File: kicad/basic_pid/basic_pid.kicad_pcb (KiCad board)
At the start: 2 copper layers, 9 parts, among them U1 LM4040LP-5, U10 OPA189, U11 BUF634A, U2 LM4040LP-5, U5 OPA189, U6 OPA189, U7 OPA189, U8 OPA189, U9 OPA189

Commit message: Schematic almost finalized:
Ended up using switches to select pre-set capacitors rather than ZIFs

TO DO:
1) design the power supply and filtering section.
2) Layout work (consider adding capacitors for stabilization...)
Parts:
- removed the U11 at (109.6, 87.7)
- added C1: 100p, Capacitor_SMD:C_0805_2012Metric, F.Cu at (130.8, 57.4)
- added C10: 100p, Capacitor_SMD:C_0805_2012Metric, F.Cu at (159.9, 130.0)
- added C11: 1n, Capacitor_SMD:C_0805_2012Metric, F.Cu at (159.9, 132.3)
- added C12: 10n, Capacitor_SMD:C_0805_2012Metric, F.Cu at (160.0, 134.6)
- added C13: 100nF, Capacitor_SMD:C_0805_2012Metric, F.Cu at (95.5, 122.0)
- added C14: 100nF, Capacitor_SMD:C_0805_2012Metric, F.Cu at (95.5, 125.0)
- added C15: 100nF, Capacitor_SMD:C_0805_2012Metric, F.Cu at (95.5, 128.0)
- added C16: 100nF, Capacitor_SMD:C_0805_2012Metric, F.Cu at (95.5, 131.0)
- added C17: 100nF, Capacitor_SMD:C_0805_2012Metric, F.Cu at (95.5, 134.1)
- added C18: 100nF, Capacitor_SMD:C_0805_2012Metric, F.Cu at (95.5, 137.1)
- added C19: 100nF, Capacitor_SMD:C_0805_2012Metric, F.Cu at (99.9, 122.0)
- added C2: 1n, Capacitor_SMD:C_0805_2012Metric, F.Cu at (130.8, 69.5)
- added C20: 100nF, Capacitor_SMD:C_0805_2012Metric, F.Cu at (99.9, 125.0)
- added C21: 100nF, Capacitor_SMD:C_0805_2012Metric, F.Cu at (99.9, 128.0)
- added C22: 100nF, Capacitor_SMD:C_0805_2012Metric, F.Cu at (99.9, 131.0)
- added C23: 100nF, Capacitor_SMD:C_0805_2012Metric, F.Cu at (99.9, 134.1)
- added C24: 100nF, Capacitor_SMD:C_0805_2012Metric, F.Cu at (99.9, 137.1)
- added C25: 100nF, Capacitor_SMD:C_0805_2012Metric, F.Cu at (104.4, 122.0)
- added C26: 100nF, Capacitor_SMD:C_0805_2012Metric, F.Cu at (104.4, 125.0)
- added C27: 100nF, Capacitor_SMD:C_0805_2012Metric, F.Cu at (104.4, 128.0)
- added C28: 100nF, Capacitor_SMD:C_0805_2012Metric, F.Cu at (104.4, 131.0)
- added C29: 100nF, Capacitor_SMD:C_0805_2012Metric, F.Cu at (104.4, 134.1)
- added C3: 10n, Capacitor_SMD:C_0805_2012Metric, F.Cu at (130.8, 75.5)
- added C30: 100nF, Capacitor_SMD:C_0805_2012Metric, F.Cu at (104.4, 137.1)
- added C31: 100nF, Capacitor_SMD:C_0805_2012Metric, F.Cu at (108.8, 122.0)
- added C32: 100nF, Capacitor_SMD:C_0805_2012Metric, F.Cu at (108.8, 125.0)
- added C33: 100nF, Capacitor_SMD:C_0805_2012Metric, F.Cu at (108.8, 128.0)
- added C34: 100nF, Capacitor_SMD:C_0805_2012Metric, F.Cu at (108.8, 131.0)
- added C35: 100n, Capacitor_SMD:C_0805_2012Metric, F.Cu at (65.7, 160.8)
- added C36: 100nF, Capacitor_SMD:C_0805_2012Metric, F.Cu at (-52.9, -24.3)
- added C37: 100nF, Capacitor_SMD:C_0805_2012Metric, F.Cu at (-52.9, -21.3)
- added C38: 100nF, Capacitor_SMD:C_0805_2012Metric, F.Cu at (63.9, 43.5)
- added C4: 100n, Capacitor_SMD:C_0805_2012Metric, F.Cu at (130.8, 81.6)
- added C5: 100p, Capacitor_SMD:C_0805_2012Metric, F.Cu at (164.7, -151.9)
- added C6: 1n, Capacitor_SMD:C_0805_2012Metric, F.Cu at (164.6, -149.7)
- added C7: 10n, Capacitor_SMD:C_0805_2012Metric, F.Cu at (164.6, -147.4)
- added C8: 100n, Capacitor_SMD:C_0805_2012Metric, F.Cu at (163.3, -145.1)
- added C9: DNP, Capacitor_SMD:C_0805_2012Metric, F.Cu at (159.9, 127.8)
- added J1: Input A, lib:BNC_Amphenol_B6252HB-NPP3G-50_Horizontal, B.Cu at (245.1, 52.6)
- added J2: Input B / Setpoint, lib:BNC_Amphenol_B6252HB-NPP3G-50_Horizontal, F.Cu at (166.2, 88.7)
- added J3: Output, lib:BNC_Amphenol_B6252HB-NPP3G-50_Horizontal, F.Cu at (183.0, 88.7)
- added J4: Output, lib:BNC_Amphenol_B6252HB-NPP3G-50_Horizontal, F.Cu at (199.7, 88.7)
- added R1: R_US, Resistor_SMD:R_0805_2012Metric, F.Cu at (65.6, 143.1)
- added R10: 10k, Resistor_SMD:R_0805_2012Metric, F.Cu at (163.7, -196.1)
- added R11: 10k, Resistor_SMD:R_0805_2012Metric, F.Cu at (384.9, -129.3)
- added R12: 220, Resistor_SMD:R_0805_2012Metric, F.Cu at (70.1, 157.8)
- added R13: 50, Resistor_SMD:R_0805_2012Metric, F.Cu at (74.5, 143.1)
- added R14: 10M, Resistor_SMD:R_0805_2012Metric, F.Cu at (178.0, -147.6)
- added R15: 10k, Resistor_SMD:R_0805_2012Metric, F.Cu at (74.5, 149.0)
- added R16: 10k, Resistor_SMD:R_0805_2012Metric, F.Cu at (74.5, 151.9)
- added R17: 10k, Resistor_SMD:R_0805_2012Metric, F.Cu at (74.5, 154.9)
- added R18: 10k, Resistor_SMD:R_0805_2012Metric, F.Cu at (74.5, 157.8)
- added R19: 50, Resistor_SMD:R_0805_2012Metric, F.Cu at (78.9, 143.1)
- added R2: R_US, Resistor_SMD:R_0805_2012Metric, F.Cu at (65.6, 146.0)
- added R20: 10k, Resistor_SMD:R_0805_2012Metric, F.Cu at (78.9, 146.0)
- added R21: 10k, Resistor_SMD:R_0805_2012Metric, F.Cu at (78.9, 149.0)
- added R22: 1M, Resistor_SMD:R_0805_2012Metric, F.Cu at (178.0, -149.9)
- added R23: 1k, Resistor_SMD:R_0805_2012Metric, F.Cu at (137.3, 129.4)
- added R24: 1k, Resistor_SMD:R_0805_2012Metric, F.Cu at (137.3, 132.4)
- added R25: 1k, Resistor_SMD:R_0805_2012Metric, F.Cu at (137.3, 135.3)
- added R26: 1k, Resistor_SMD:R_0805_2012Metric, F.Cu at (137.3, 138.3)
- added R27: 1k, Resistor_SMD:R_0805_2012Metric, F.Cu at (137.3, 141.2)
- added R28: 10, Resistor_SMD:R_0805_2012Metric, F.Cu at (-65.8, -24.3)
- added R29: 10, Resistor_SMD:R_0805_2012Metric, F.Cu at (-65.8, -21.4)
- added R3: 10k, Resistor_SMD:R_0805_2012Metric, F.Cu at (65.6, 149.0)
- added R30: 10k, Resistor_SMD:R_0805_2012Metric, F.Cu at (-65.8, -18.4)
- added R31: 10k, Resistor_SMD:R_0805_2012Metric, F.Cu at (-65.8, -15.5)
- added R32: 10k, Resistor_SMD:R_0805_2012Metric, F.Cu at (-65.8, -12.5)
- added R33: 10k, Resistor_SMD:R_0805_2012Metric, F.Cu at (72.0, 28.4)
- added R34: 1k, Resistor_SMD:R_0805_2012Metric, F.Cu at (51.0, 52.2)
- added R4: 10k, Resistor_SMD:R_0805_2012Metric, F.Cu at (65.6, 151.9)
- added R5: 10k, Resistor_SMD:R_0805_2012Metric, F.Cu at (65.6, 154.9)
- added R6: 10k, Resistor_SMD:R_0805_2012Metric, F.Cu at (65.6, 157.8)
- added R7: 10k, Resistor_SMD:R_0805_2012Metric, F.Cu at (70.1, 143.1)
- added R8: 10k, Resistor_SMD:R_0805_2012Metric, F.Cu at (70.1, 146.0)
- added R9: 10k, Resistor_SMD:R_0805_2012Metric, F.Cu at (70.1, 149.0)
- added RV1: 100k, lib:Slide_pot_45mm, B.Cu at (45.7, 149.4)
- added RV2: 100k, lib:Slide_pot_45mm, B.Cu at (170.9, -168.4)
- added RV3: 100k, lib:Slide_pot_45mm, B.Cu at (391.9, -101.9)
- added RV4: 100k, lib:Slide_pot_45mm, F.Cu at (238.6, 124.6)
- added RV5: 100k, lib:Slide_pot_45mm, F.Cu at (250.7, 124.6)
- added RV6: 100k, lib:Slide_pot_45mm, F.Cu at (58.4, 151.1)
- added RV7: 10K, Potentiometer_THT:Potentiometer_Bourns_3296W_Vertical, F.Cu at (-60.5, -4.93)
- added RV9: 10K, Potentiometer_THT:Potentiometer_Bourns_3296W_Vertical, F.Cu at (61.0, 23.9)
- added SW1: SW_DPDT_x2, lib:MHS222, B.Cu at (245.9, 60.1)
- added SW10: SW_DPDT_x2, lib:MHS222, F.Cu at (58.3, 31.5)
- added SW2: SW_DPDT_x2, lib:MHS222, F.Cu at (193.9, 133.0)
- added SW4: SW_SP4T, lib:SLB1470, F.Cu at (144.2, 102.5)
- added SW6: SW_SP4T, lib:SLB1470, F.Cu at (150.3, 102.5)
- added SW7: SW_SP4T, lib:SLB1470, B.Cu at (160.0, -148.5)
- added SW8: SW_SP4T, lib:SLB1470, B.Cu at (181.3, -148.6)
- added SW9: SW_SP4T, lib:SLB1470, F.Cu at (155.4, 131.3)
- added U13: BUF634A, lib:TI_SO-PowerPAD-8_ThermalVias, F.Cu at (162.3, 139.1)
- added U14: OPA189, Package_SO:SOIC-8_3.9x4.9mm_P1.27mm, F.Cu at (-59.4, -22.6)
- added U15: OPA189, Package_SO:SOIC-8_3.9x4.9mm_P1.27mm, F.Cu at (-59.4, -16.1)
- added U3: LT1167, Package_DIP:DIP-8_W7.62mm_LongPads, B.Cu at (241.8, 66.8)
- added U4: LT1167, Package_DIP:DIP-8_W7.62mm_LongPads, F.Cu at (181.6, 94.0)
- added U7: OPA189, Package_SO:SOIC-8_3.9x4.9mm_P1.27mm, F.Cu at (172.3, 106.9)
- added U8: BUF634A, lib:TI_SO-PowerPAD-8_ThermalVias, F.Cu at (163.7, 101.7)
- moved U10 362.8 mm to (390.0, -123.3), turned to -90 degrees
- moved U9 245.7 mm to (170.3, -146.6), turned to 90 degrees
- moved U5 83.3 mm to (45.5, 138.6)
- moved U12 72.0 mm to (162.4, 145.4)
- renumbered U8 to U10, U9 to U11, U10 to U12, U7 to U9
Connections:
- U12 pad 4: VS -> Vlim-
- U12 pad 7: VD -> Vlim+
- U5 pad 6: Net-(U5--) -> Internal_setpoint
- U6 pad 6: Net-(J3-In) -> Error_signal
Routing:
- net Net-(SW7-Common): track 0.00 -> 58.4 mm
- net Net-(R17-Pad1): track 0.00 -> 47.0 mm, vias 0 -> 2
- net Net-(C5-Pad1): track 0.00 -> 36.6 mm
- net Net-(J1-In): track 0.00 -> 23.8 mm
- net Net-(J1-Ext): track 0.00 -> 20.3 mm
- net Net-(SW1A-B): track 0.00 -> 10.2 mm
- net Net-(U10--): track 0.00 -> 8.44 mm
- net Net-(SW1B-B): track 0.00 -> 6.28 mm
- net Net-(C5-Pad2): track 0.00 -> 3.71 mm
- net Net-(C6-Pad2): track 0.00 -> 3.69 mm
- net Net-(C7-Pad2): track 0.00 -> 3.64 mm
- net Net-(R14-Pad1): track 0.00 -> 2.44 mm
- net Net-(R22-Pad1): track 0.00 -> 2.43 mm
- net Net-(C8-Pad2): track 0.00 -> 2.36 mm
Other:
- copper layers 2 -> 4

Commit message: Schematic finalized and layout work begun
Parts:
- removed RV9: 10K, Potentiometer_THT:Potentiometer_Bourns_3296W_Vertical
- added C39: 100nF, Capacitor_SMD:C_0805_2012Metric, F.Cu at (156.2, 184.9)
- added C40: 100nF, Capacitor_SMD:C_0805_2012Metric, F.Cu at (148.7, 214.6)
- added C41: 100nF, Capacitor_SMD:C_0805_2012Metric, F.Cu at (49.4, 67.7)
- added C42: 10uF, Capacitor_SMD:C_1210_3225Metric, F.Cu at (54.4, 68.3)
- added C43: 100nF, Capacitor_SMD:C_0805_2012Metric, F.Cu at (49.4, 70.7)
- added C44: 22uF, Capacitor_SMD:CP_Elec_4x5.8, F.Cu at (51.0, 63.3)
- added D1: GBU4A, Diode_THT:Diode_Bridge_Vishay_GBU, F.Cu at (118.6, 199.9)
- added H1: MountingHole, MountingHole:MountingHole_3.2mm_M3_ISO14580, F.Cu at (101.6, 29.6)
- added H2: MountingHole, MountingHole:MountingHole_3.2mm_M3_ISO14580, F.Cu at (101.6, 36.7)
- added H3: MountingHole, MountingHole:MountingHole_3.2mm_M3_ISO14580, F.Cu at (101.6, 43.8)
- added H4: MountingHole, MountingHole:MountingHole_3.2mm_M3_ISO14580, F.Cu at (101.6, 50.8)
- added J5: Screw_Terminal_01x04, TerminalBlock:TerminalBlock_Altech_AK300-4_P5.00mm, F.Cu at (35.1, 55.5)
- added J6: Screw_Terminal_01x03, TerminalBlock:TerminalBlock_Altech_AK300-3_P5.00mm, F.Cu at (73.6, 57.9)
- added SW3: SW_DPDT_x2, lib:MHS222, F.Cu at (40.1, 81.6)
- added SW5: SW_DPDT_x2, lib:MHS222, F.Cu at (40.1, 90.6)
- added U16: LM317_TO-252, Package_TO_SOT_SMD:TO-252-2, F.Cu at (41.9, 64.4)
- C1: value 100p -> 100n
- C10: value 100p -> DNP
- C11: value 1n -> 100p
- C12: value 10n -> 1n
- C13: value 100nF -> 10n
- C18, C19: value 100nF -> 22mF; footprint Capacitor_SMD:C_0805_2012Metric -> Capacitor_THT:CP_Radial_D30.0mm_P10.00mm_SnapIn
- C2: value 1n -> DNP
- C24, C25: value 100nF -> 10uF; footprint Capacitor_SMD:C_0805_2012Metric -> Capacitor_SMD:C_1210_3225Metric
- C3: value 10n -> 100p
- C32, C33: value 100nF -> 220uF; footprint Capacitor_SMD:C_0805_2012Metric -> Capacitor_SMD:CP_Elec_8x6.9
- C35, C8: value 100n -> 100nF
- C4: value 100n -> 1n
- C5: value 100p -> 10n
- C6: value 1n -> 1nF
- C7: value 10n -> 10nF
- C9: value DNP -> 1uF
- J1, J3, J4: footprint lib:BNC_Amphenol_B6252HB-NPP3G-50_Horizontal -> lib:BNC_Amphenol_031-5539_Vertical
- J2: footprint lib:BNC_Amphenol_B6252HB-NPP3G-50_Horizontal -> lib:BNC_Amphenol_031-5539_Vertical; moved to B.Cu
- R12: value 220 -> 10k
- R13, R19: value 50 -> 10k
- R14: value 10M -> 220
- R15: value 10k -> 50
- R16: value 10k -> 1M
- R17: value 10k -> 10M
- R22: value 1M -> 10k
- R23: value 1k -> 50
- R28: value 10 -> 1k
- R29: value 10 -> DNP
- R30, R31: value 10k -> 1k
- R32: value 10k -> 330
- R33: value 10k -> DNP
- R34: value 1k -> DNP
- RV6: value 100k -> 10K; footprint lib:Slide_pot_45mm -> Potentiometer_THT:Potentiometer_Bourns_3296W_Vertical
- RV7: value 10K -> 2k
- SW2, U4: moved to B.Cu
- U14: value OPA189 -> LM2940CS-12/NOPB; footprint Package_SO:SOIC-8_3.9x4.9mm_P1.27mm -> Package_TO_SOT_SMD:TO-263-3_TabPin2
- U15: value OPA189 -> LM2990SX-12; footprint Package_SO:SOIC-8_3.9x4.9mm_P1.27mm -> Package_TO_SOT_SMD:TO-263-3_TabPin2
- moved C37 282.5 mm to (93.7, 220.1)
- moved U15 277.7 mm to (125.2, 191.3)
- moved U14 273.3 mm to (125.2, 179.0)
- moved C36 258.5 mm to (93.7, 188.6)
- moved RV3 243.0 mm to (195.0, 40.4)
- moved R11 243.0 mm to (188.0, 13.0)
- moved U10 243.0 mm to (193.1, 19.0)
- moved C5 207.5 mm to (152.6, 55.2)
- moved C6 207.5 mm to (152.6, 57.4)
- moved C7 207.5 mm to (152.5, 59.8)
- moved C8 207.5 mm to (151.3, 62.1)
- moved R10 207.5 mm to (151.6, 11.0)
- moved R14 207.5 mm to (165.9, 59.6)
- moved R22 207.5 mm to (165.9, 57.3)
- moved RV2 207.5 mm to (158.8, 38.7)
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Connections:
- C1 pad 1: Net-(SW5-B) -> GND
- C13 pad 1: VD -> Net-(U13-OUT)
- C13 pad 2: GND -> Net-(C13-Pad2)
- C14 pad 1: GND -> +12V
- C14 pad 2: VS -> GND
- C15 pad 1: VD -> GND
- C15 pad 2: GND -> -12V
- C16 pad 1: GND -> +12V
- C16 pad 2: VS -> GND
- C17 pad 1: VD -> GND
- C17 pad 2: GND -> -12V
- C18 pad 1: GND -> V+_unreg
- C18 pad 2: VS -> GND
- C19 pad 1: VD -> GND
- C19 pad 2: GND -> Net-(D1--)
- C2 pad 1: Net-(SW5-B) -> Net-(SW3A-B)
- C20 pad 1: GND -> +12V
- C20 pad 2: VS -> GND
- C21 pad 1: VD -> GND
- C21 pad 2: GND -> -12V
- C22 pad 1: GND -> +12V
- C22 pad 2: VS -> GND
- C23 pad 1: VD -> GND
- C23 pad 2: GND -> -12V
- C24 pad 1: GND -> V+_unreg
- C24 pad 2: VS -> GND
- C25 pad 1: VD -> GND
- C25 pad 2: GND -> Net-(D1--)
- C26 pad 1: GND -> +12V
- C26 pad 2: VS -> GND
- C27 pad 1: VD -> GND
- C27 pad 2: GND -> -12V
- C28 pad 1: GND -> +12V
- C28 pad 2: VS -> GND
- C29 pad 1: VD -> GND
- C29 pad 2: GND -> -12V
- C3 pad 1: Net-(SW5-B) -> Net-(SW3A-B)
- C30 pad 1: GND -> +12V
- C30 pad 2: VS -> GND
- C31 pad 1: VD -> GND
- C31 pad 2: GND -> -12V
- C32 pad 1: GND -> +12V
- C32 pad 2: VS -> GND
- C33 pad 1: VD -> GND
- C33 pad 2: GND -> -12V
- C34 pad 1: GND -> +12V
- C34 pad 2: VS -> GND
- C35 pad 2: Net-(C35-Pad2) -> -12V
- C36 pad 1: Net-(C36-Pad1) -> +12V
- C36 pad 2: unconnected-(C36-Pad2) -> GND
- C37 pad 1: Net-(C37-Pad1) -> GND
- C37 pad 2: unconnected-(C37-Pad2) -> -12V
- C38 pad 1: Vlim- -> +12V
- C4 pad 1: Net-(SW5-B) -> Net-(SW3A-B)
- C5 pad 1: Net-(C5-Pad1) -> Net-(SW3A-B)
- C6 pad 1: Net-(C5-Pad1) -> Net-(C6-Pad1)
- C7 pad 1: Net-(C5-Pad1) -> Net-(C6-Pad1)
- C8 pad 1: Net-(C5-Pad1) -> Net-(C6-Pad1)
- C9 pad 1: Net-(U13-OUT) -> Net-(C6-Pad1)
- R1 pad 2: VD -> +12V
- R10 pad 1: Error_signal -> Net-(R10-Pad1)
- R10 pad 2: Net-(R10-Pad2) -> Error_signal
- R11 pad 1: Error_signal -> Net-(R11-Pad1)
- R11 pad 2: Net-(U10--) -> Net-(R10-Pad1)
- R12 pad 1: Net-(SW6-Common) -> Error_signal
- R12 pad 2: Net-(U11--) -> Net-(R12-Pad2)
- R13 pad 1: Net-(U7--) -> Error_signal
- R13 pad 2: Net-(J3-In) -> Net-(U10--)
- R14 pad 1: Net-(R14-Pad1) -> Net-(SW6-Common)
- R14 pad 2: Net-(C5-Pad1) -> Net-(U11--)
- R15 pad 1: Net-(R15-Pad1) -> Net-(U7--)
- R15 pad 2: Net-(SW9-Common) -> Net-(J3-In)
- R16 pad 1: Net-(C5-Pad1) -> Net-(R16-Pad1)
- R16 pad 2: Net-(SW9-Common) -> Net-(C6-Pad1)
- R17 pad 2: Net-(SW9-Common) -> Net-(C6-Pad1)
- R18 pad 1: Net-(SW9-Common) -> Net-(R18-Pad1)
- R18 pad 2: Net-(U13-OUT) -> Net-(SW9-Common)
- R19 pad 1: Net-(U13-OUT) -> Net-(C6-Pad1)
- R19 pad 2: Net-(J4-In) -> Net-(SW9-Common)
- R2 pad 1: VS -> -12V
- R20 pad 1: Net-(U5--) -> Net-(R20-Pad1)
- R20 pad 2: Internal_setpoint -> Net-(SW9-Common)
- R21 pad 1: GND -> Net-(SW9-Common)
- R21 pad 2: Net-(U5--) -> Positive_offset
- R22 pad 1: Net-(R22-Pad1) -> Net-(SW9-Common)
- R22 pad 2: Net-(C5-Pad1) -> Net-(U13-OUT)
- R23 pad 1: Net-(R23-Pad1) -> Net-(U13-OUT)
- R23 pad 2: VD -> Net-(J4-In)
- R24 pad 2: VD -> +12V
- R25 pad 2: VD -> +12V
- R26 pad 1: VS -> Net-(R26-Pad1)
- R26 pad 2: Net-(R26-Pad2) -> +12V
- R27 pad 1: VS -> -12V
- R28 pad 1: Net-(C36-Pad1) -> -12V
- R29 pad 1: Net-(C37-Pad1) -> -12V
- R29 pad 2: Net-(U15--) -> Net-(SW10A-C)
- R3 pad 1: Net-(C35-Pad2) -> Net-(C1-Pad2)
- R30 pad 1: VD -> Net-(R30-Pad1)
- R30 pad 2: Net-(R30-Pad2) -> Net-(U16-ADJ)
- R31 pad 1: Net-(R28-Pad2) -> -12V
- R31 pad 2: Net-(U14--) -> Vlim-
- R32 pad 1: Net-(U14--) -> Net-(U16-ADJ)
- R32 pad 2: GND -> Vlim+
- R33 pad 1: Net-(SW9-Common) -> Net-(R33-Pad1)
- R33 pad 2: Positive_offset -> Net-(R33-Pad2)
- R34 pad 1: VS -> Net-(R34-Pad1)
- R34 pad 2: Vlim- -> Net-(R34-Pad2)
- R4 pad 1: Input_B -> GND
- R4 pad 2: Net-(U6-+) -> Net-(U5--)
- R5 pad 1: Internal_setpoint -> Net-(U5--)
- R5 pad 2: Net-(U6-+) -> Internal_setpoint
- R6 pad 1: Input_A -> Input_B
- R7 pad 1: GND -> Internal_setpoint
- R7 pad 2: Net-(U6--) -> Net-(U6-+)
- R8 pad 1: Net-(R8-Pad1) -> Input_A
- R8 pad 2: Error_signal -> Net-(U6-+)
- R9 pad 1: Net-(R9-Pad1) -> GND
- R9 pad 2: Net-(R8-Pad1) -> Net-(U6--)
- RV1 pad 1: Net-(R9-Pad1) -> Net-(U1-K)
- RV1 pad 2: Net-(U6--) -> Net-(C1-Pad2)
- RV1 pad 3: Net-(U6--) -> Net-(U2-A)
- RV1 pad A: Net-(R23-Pad1) -> GND
- RV1 pad C: GND -> Net-(R28-Pad2)
- RV2 pad 1: Net-(R10-Pad2) -> Net-(R11-Pad1)
- RV2 pad 2: Net-(R10-Pad2) -> Net-(U6--)
- RV2 pad 3: Net-(SW7-Common) -> Net-(U6--)
- RV3 pad 1: Net-(U10--) -> Net-(R12-Pad2)
- RV3 pad 2: Net-(U10--) -> Net-(R12-Pad2)
- RV3 pad 3: Net-(R17-Pad1) -> Net-(SW7-Common)
- RV4 pad 1: Net-(R15-Pad1) -> Net-(U10--)
- RV4 pad 2: Net-(U11--) -> Net-(U10--)
- RV4 pad 3: Net-(U11--) -> Net-(R20-Pad1)
- RV4 pad A: GND -> Net-(R26-Pad1)
- RV4 pad C: Net-(R26-Pad2) -> GND
- RV5 pad 1: (no net) -> Net-(R18-Pad1)
- RV5 pad 2: (no net) -> Net-(U11--)
- RV5 pad 3: (no net) -> Net-(U11--)
- RV6 pad 1: Net-(U1-K) -> GND
- RV6 pad 2: Net-(C35-Pad2) -> Net-(SW10A-C)
- RV6 pad 3: Net-(U2-A) -> -12V
- RV7 pad 1: Net-(R30-Pad2) -> Net-(R30-Pad1)
- RV7 pad 2: Net-(U15-+) -> GND
- RV7 pad 3: VS -> GND
- SW10 pad 4: VS -> -12V
- SW2 pad 3: unconnected-(SW2A-C-Pad3) -> Net-(J2-Ext)
- SW2 pad S: unconnected-(SW2-PadS) -> GND
- SW6 pad 1: Net-(C1-Pad2) -> Net-(C2-Pad2)
- SW6 pad 2: Net-(C2-Pad2) -> Net-(C3-Pad2)
- SW6 pad 3: Net-(C3-Pad2) -> Net-(C4-Pad2)
- SW6 pad 4: Net-(C4-Pad2) -> Net-(C5-Pad2)
- SW7 pad 1: Net-(C5-Pad2) -> Net-(C6-Pad2)
- SW7 pad 2: Net-(C6-Pad2) -> Net-(C7-Pad2)
- SW7 pad 3: Net-(C7-Pad2) -> Net-(C8-Pad2)
- SW7 pad 4: Net-(C8-Pad2) -> Net-(C9-Pad2)
- SW8 pad 1: Net-(C5-Pad1) -> Net-(C6-Pad1)
- SW8 pad 2: Net-(R22-Pad1) -> Net-(R16-Pad1)
- SW8 pad 3: Net-(R14-Pad1) -> Net-(R17-Pad1)
- SW9 pad 1: Net-(C9-Pad2) -> Net-(C10-Pad2)
- SW9 pad 2: Net-(C10-Pad2) -> Net-(C11-Pad2)
- SW9 pad 3: Net-(C11-Pad2) -> Net-(C12-Pad2)
- SW9 pad 4: Net-(C12-Pad2) -> Net-(C13-Pad2)
- U10 pad 4: VS -> -12V
- U10 pad 6: Net-(R17-Pad1) -> Net-(R20-Pad1)
- U10 pad 7: VD -> +12V
- U11 pad 4: VS -> -12V
- U11 pad 6: Net-(R15-Pad1) -> Net-(R18-Pad1)
- U11 pad 7: VD -> +12V
- U13 pad 4: VS -> -12V
- U13 pad 7: VD -> +12V
- U13 pad 9: VS -> -12V
- U14 pad 1: unconnected-(U14-NC-Pad1) -> V+_unreg
- U14 pad 2: Net-(U14--) -> GND
- U14 pad 3: unconnected-(U14-+-Pad3) -> +12V
- U15 pad 1: unconnected-(U15-NC-Pad1) -> GND
- U15 pad 2: Net-(U15--) -> Net-(D1--)
- U15 pad 3: Net-(U15-+) -> -12V
- U3 pad 1: unconnected-(U3-Rg-Pad1) -> Net-(R33-Pad2)
- U3 pad 4: VS -> -12V
- U3 pad 7: VD -> +12V
- U3 pad 8: unconnected-(U3-Rg-Pad8) -> Net-(R33-Pad1)
- U4 pad 1: unconnected-(U4-Rg-Pad1) -> Net-(R34-Pad2)
- U4 pad 4: VS -> -12V
- U4 pad 7: VD -> +12V
- U4 pad 8: unconnected-(U4-Rg-Pad8) -> Net-(R34-Pad1)
- U5 pad 4: VS -> -12V
- U5 pad 7: VD -> +12V
- U6 pad 4: VS -> -12V
- U6 pad 7: VD -> +12V
- U7 pad 4: VS -> -12V
- U7 pad 7: VD -> +12V
- U8 pad 4: VS -> -12V
- U8 pad 7: VD -> +12V
- U8 pad 9: VS -> -12V
- U9 pad 4: VS -> -12V
- U9 pad 6: Net-(C5-Pad1) -> Net-(C6-Pad1)
- U9 pad 7: VD -> +12V
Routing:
- net Net-(R17-Pad1): track 47.0 -> 0.00 mm, vias 2 -> 0
- net Net-(SW7-Common): track 58.4 -> 105.4 mm, vias 0 -> 2
- net (no net): track 0.00 -> 39.0 mm
- net Net-(C5-Pad1): track 36.6 -> 0.00 mm
- net Net-(J2-In): track 0.00 -> 34.4 mm
- net Net-(J2-Ext): track 0.00 -> 30.7 mm
- net Net-(SW2A-B): track 0.00 -> 9.98 mm
- net Net-(J1-Ext): track 20.3 -> 30.2 mm
- net Net-(J1-In): track 23.8 -> 33.7 mm
- net Net-(SW2B-B): track 0.00 -> 6.24 mm
- net Net-(R33-Pad1): track 0.00 -> 3.05 mm
- net Net-(R34-Pad1): track 0.00 -> 3.02 mm
- net Net-(R34-Pad2): track 0.00 -> 2.78 mm
- net Net-(R33-Pad2): track 0.00 -> 2.75 mm
- net Net-(R14-Pad1): track 2.44 -> 0.00 mm
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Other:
- board outline added: 152.4 x 76.2 mm

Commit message: Layout almost completed
This is an almost completed snapshot of the layout. Here what to do:

1) Make sure that when flipped the back has sliders on the bottom: this will require
   reversing the direction of increasing gain with consequent shortening of certain
   signal traces

2) Fix the position of connectors, sliders and switches to "reasonable locations"
3) Make a verbose silkscreen (expecially on bottom) showing all functions.
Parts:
- removed C41: 100nF, Capacitor_SMD:C_0805_2012Metric
- J3, J4, RV4, RV5, RV6, RV7, SW10, SW4, SW5, SW6, SW9: moved to B.Cu
- U1, U2: value LM4040LP-5 -> LM4040DBZ-5; footprint Package_TO_SOT_THT:TO-92_Inline -> Package_TO_SOT_SMD:SOT-23
- moved J2 192.6 mm to (37.7, 113.2), turned to 90 degrees
- moved R33 179.8 mm to (67.2, 113.2), turned to 0 degrees
- moved U3 177.1 mm to (70.8, 113.2), turned to 180 degrees
- moved SW1 176.1 mm to (78.1, 113.3), turned to 90 degrees
- moved D1 174.5 mm to (43.3, 42.5)
- moved U15 171.9 mm to (32.7, 46.4), turned to 90 degrees
- moved SW2 171.6 mm to (54.0, 113.4), turned to -90 degrees
- moved R31 170.7 mm to (201.9, 93.9), turned to 90 degrees
- moved J1 167.0 mm to (95.0, 113.8), turned to -90 degrees
- moved R29 166.7 mm to (198.7, 80.3), turned to -90 degrees
- moved U4 159.4 mm to (60.3, 109.0), turned to 0 degrees
- moved RV6 158.2 mm to (201.3, 83.2)
- moved SW10 155.9 mm to (202.8, 89.9), turned to 180 degrees
- moved R34 154.9 mm to (64.0, 109.0), turned to 180 degrees
- moved RV4 143.7 mm to (111.2, 57.9), turned to 180 degrees
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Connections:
- C40 pad 1: +12V -> Vlim+
- J6 pad 1: V+_unreg -> Net-(D1--)
- J6 pad 3: Net-(D1--) -> V+_unreg
- RV1 pad 1: Net-(U1-K) -> Net-(U2-A)
- RV1 pad 3: Net-(U2-A) -> Net-(U1-K)
- RV2 pad 1: Net-(R11-Pad1) -> Net-(U6--)
- RV2 pad 3: Net-(U6--) -> Net-(R11-Pad1)
- RV5 pad 1: Net-(R18-Pad1) -> Net-(U11--)
- RV5 pad 3: Net-(U11--) -> Net-(R18-Pad1)
- U1 pad 1: (no net) -> Net-(U1-K)
- U1 pad 2: Net-(U1-K) -> GND
- U1 pad 3: GND -> (no net)
- U2 pad 1: (no net) -> GND
- U2 pad 2: GND -> Net-(U2-A)
- U2 pad 3: Net-(U2-A) -> (no net)
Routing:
- net Input_A: track 0.00 -> 179.7 mm, vias 0 -> 2
- net Input_B: track 0.00 -> 136.3 mm
- net V+_unreg: track 0.00 -> 136.2 mm, vias 0 -> 2
- net Internal_setpoint: track 0.00 -> 106.2 mm, vias 0 -> 2
- net Net-(R20-Pad1): track 0.00 -> 91.6 mm, vias 0 -> 1
- net Net-(D1--): track 0.00 -> 76.4 mm
- net Net-(C6-Pad1): track 0.00 -> 70.9 mm
- net Net-(SW7-Common): track 105.4 -> 43.4 mm, vias 2 -> 0
- net Vlim+: track 0.00 -> 61.8 mm, vias 0 -> 2
- net Net-(U11--): track 0.00 -> 57.4 mm, vias 0 -> 2
- net +12V: track 0.00 -> 47.2 mm, vias 0 -> 16
- net -12V: track 0.00 -> 43.8 mm, vias 0 -> 16
- net Error_signal: track 0.00 -> 43.7 mm
- net Net-(SW5A-B): track 0.00 -> 39.1 mm
- net (no net): track 39.0 -> 0.00 mm
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- added copper zone on B.Cu, net +12V
- added copper zone on In2.Cu, net -12V
- added copper zone on F.Cu, net GND
- added copper zone on In1.Cu, net GND
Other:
- board size 152.4 x 76.2 mm -> 152.4 x 101.6 mm

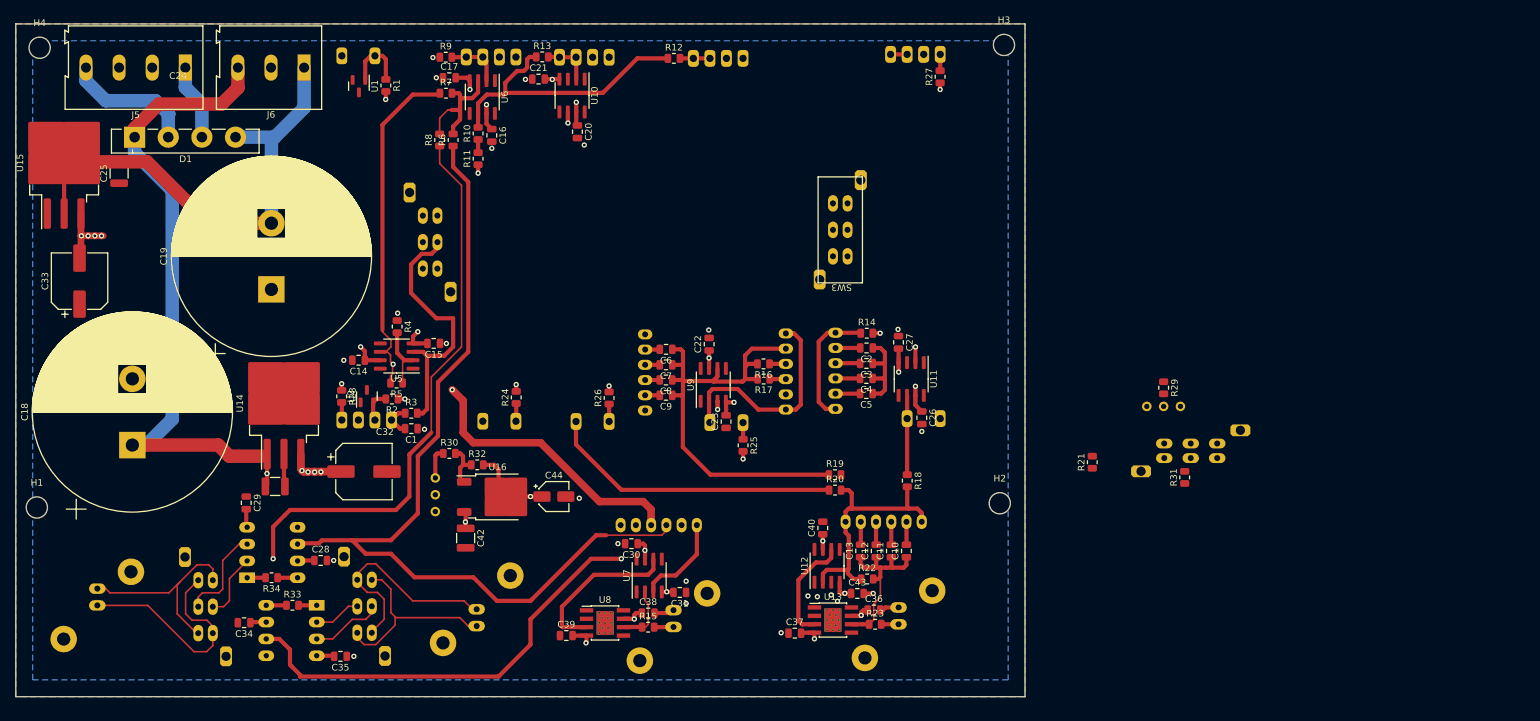
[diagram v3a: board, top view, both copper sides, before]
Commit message: Board is functionally operational but requires more reviews:
TO DO list
    1) Substitute input op-amps with an INA849: that should give higher bandwidth
    2) Make sure that when flipped the back has sliders on the bottom: this will require
       reversing the direction of increasing gain with consequent shortening of certain
       signal traces

    3) Fix the position of connectors, sliders and switches to "reasonable locations"
    4) Make a verbose silkscreen (expecially on bottom) showing all functions.
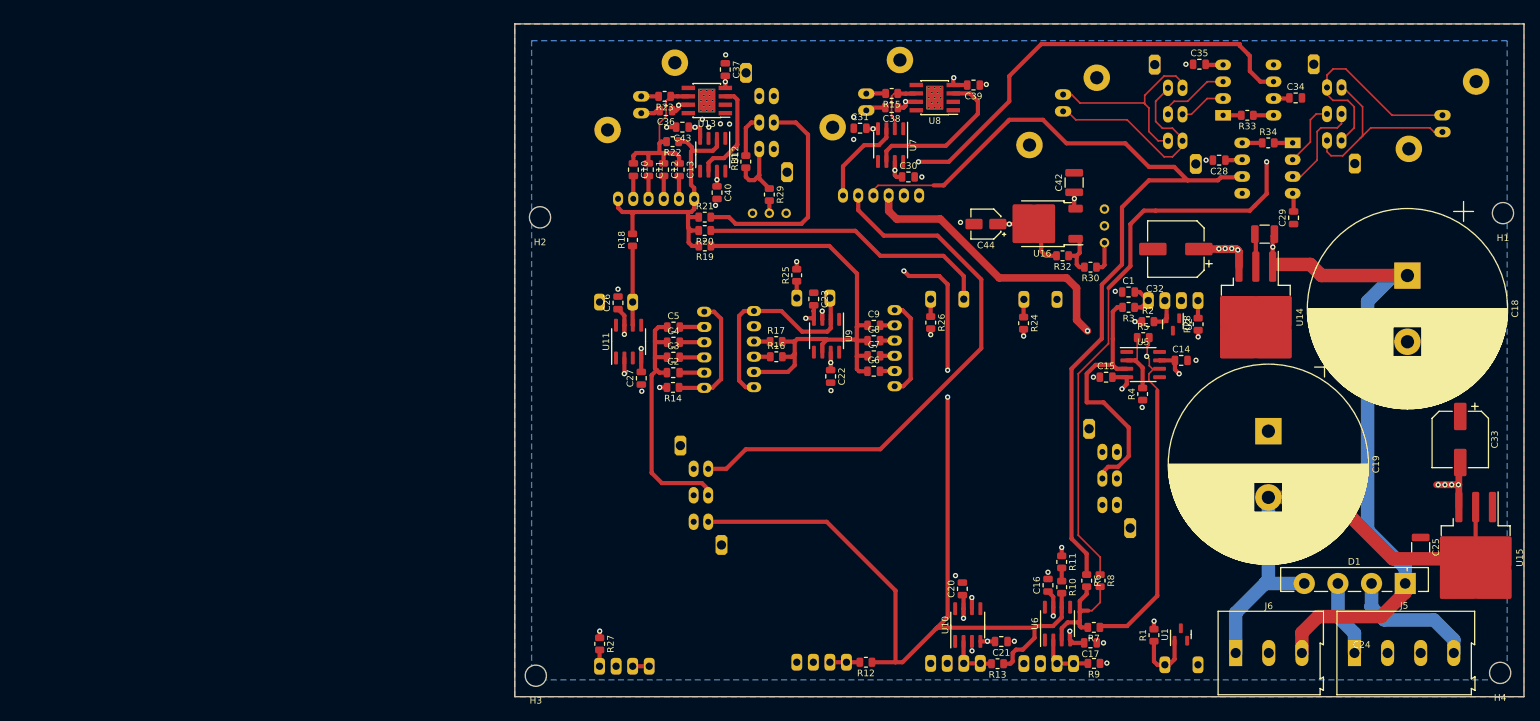
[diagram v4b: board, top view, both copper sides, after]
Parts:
- J3: value Output -> Monitor
- SW3: moved to B.Cu
- moved H4 239.9 mm to (249.6, 123.4), turned to 180 degrees
- moved H1 225.8 mm to (250.0, 54.0), turned to 180 degrees
- moved U15 221.3 mm to (245.9, 106.0), turned to -90 degrees
- moved J2 216.2 mm to (240.8, 39.2), turned to -90 degrees
- moved C33 209.9 mm to (243.5, 88.2), turned to -90 degrees
- moved C25 204.5 mm to (237.6, 104.4), turned to -90 degrees
- moved D1 203.4 mm to (235.2, 109.9), turned to 180 degrees
- moved J5 197.4 mm to (227.6, 120.4), turned to 0 degrees
- moved C18 194.2 mm to (235.6, 63.4), turned to -90 degrees
- moved SW2 186.0 mm to (224.5, 39.0), turned to 90 degrees
- moved C34 177.5 mm to (218.7, 36.6), turned to 0 degrees
- moved U4 171.0 mm to (218.2, 43.4), turned to 180 degrees
- moved J6 166.1 mm to (209.6, 120.4), turned to 0 degrees
- moved R34 164.2 mm to (214.5, 43.4), turned to 0 degrees
- moved C29 163.9 mm to (218.4, 54.7), turned to 90 degrees
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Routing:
- net Error_signal: track 43.7 -> 158.7 mm, vias 0 -> 3
- net Input_A: track 179.7 -> 264.0 mm
- net Positive_offset: track 0.00 -> 34.0 mm
- net Net-(SW3A-B): track 13.6 -> 40.0 mm
- net Net-(SW10A-C): track 0.00 -> 24.9 mm
- net Vlim-: track 3.32 -> 21.4 mm
- net Net-(SW7-Common): track 43.4 -> 58.3 mm
- net -12V: track 43.8 -> 52.3 mm
- net Net-(SW9-Common): track 38.1 -> 43.8 mm
- net Vlim+: track 61.8 -> 65.6 mm
- net Net-(U13-IN): track 16.4 -> 15.6 mm
- net Net-(U8-IN): track 24.4 -> 23.8 mm
- net GND: vias 24 -> 27
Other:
- board text added: "Derivative"
- board text added: "General gain"
- board text added: "Integral"
- board text added: "Manual setpoint"
- board text added: "Proportional"
